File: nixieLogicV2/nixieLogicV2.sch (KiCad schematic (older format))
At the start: 42 parts, among them J1 GPS, J2 Conn_01x10_Female, J3 Barrel_Jack, Q1 2sk3234, SW1 SW_Push, SW2 SW_Push, SW3 SW, SW4 SW, SW5 SW, SW6 SW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

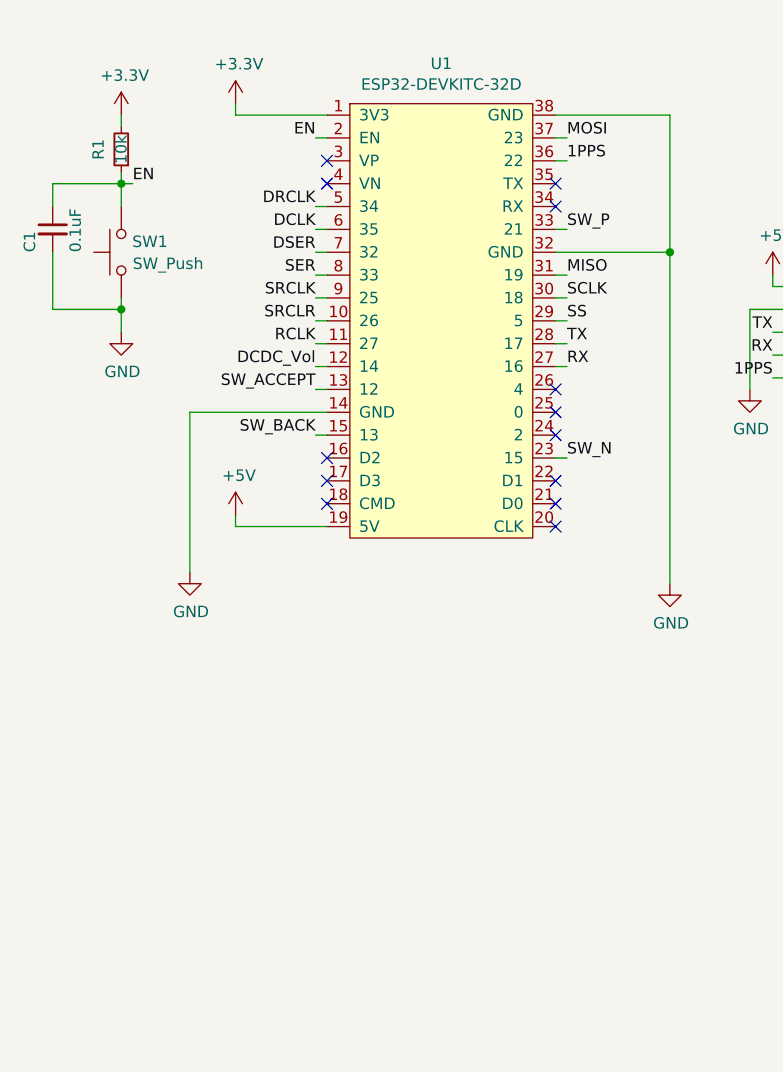
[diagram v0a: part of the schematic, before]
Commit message: add FirmWare Currently Ntp Function working need to add config menu
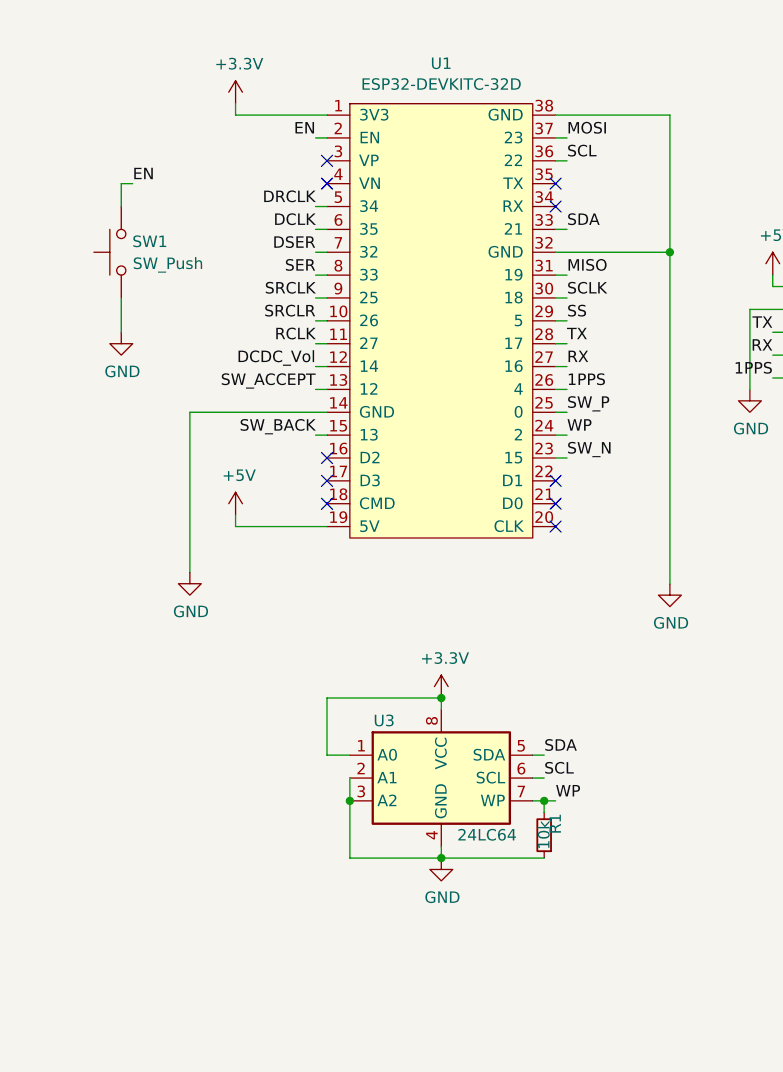
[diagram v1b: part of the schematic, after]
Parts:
- removed C1: 0.1uF, Capacitor_SMD:C_0805_2012Metric_Pad1.15x1.40mm_HandSolder, symbol Device:C_Small
- added U3: 24LC64, Package_DIP:DIP-8_W7.62mm_Socket_LongPads, symbol Memory_EEPROM:24LC64
- D2: footprint Package_TO_SOT_THT:TO-220-2_Horizontal_TabUp -> Package_TO_SOT_THT:TO-220-2_Horizontal_TabDown
- Q1: footprint Package_TO_SOT_THT:TO-220F-3_Horizontal_TabUp -> Package_TO_SOT_THT:TO-220-3_Horizontal_TabDown
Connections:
- net +3V3: now also U3.1 (A0), U3.8 (VCC); no longer R1.2
- net 1PPS: now also U1.26 (4); no longer U1.36 (22)
- net EN: no longer R1.1
- net GND: now also R1.1, U3.2 (A1), U3.3 (A2), U3.4 (GND)
- net SW_P: now also U1.25 (0); no longer U1.33 (21)
- net WP: now reaches U1.24 (2)
- net WP: now also R1.2, U3.7 (WP)
- new net SCL: U1.36 (22), U3.6 (SCL)
- new net SDA: U1.33 (21), U3.5 (SDA)
- no-connect marks 16 -> 13
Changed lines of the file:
@@
 	0    -1   -1   0
 $EndComp
-$Comp
-L Device:C_Small C1
-U 1 1 5FC003DB
-P 4850 1450
-F 0 "C1" V 4750 1350 50  0000 L CNN
-F 1 "0.1uF" V 4950 1350 50  0000 L CNN
-F 2 "Capacitor_SMD:C_0805_2012Metric_Pad1.15x1.40mm_HandSolder" H 4850 1450 50  0001 C CNN
-F 3 "~" H 4850 1450 50  0001 C CNN
-	1    4850 1450
-	1    0    0    -1
-$EndComp
-Wire Wire Line
-	4850 1350 4850 1250
-Wire Wire Line
-	4850 1250 5150 1250
-Wire Wire Line
-	5150 1250 5150 1200
 Wire Wire Line
 	5150 1350 5150 1250
-Connection ~ 5150 1250
-Wire Wire Line
-	4850 1800 5150 1800
-Wire Wire Line
-	5150 1800 5150 1750
 $Comp
 L power:GND #PWR02
@@
 $EndComp
 Wire Wire Line
-	5150 1900 5150 1800
-Connection ~ 5150 1800
-Wire Wire Line
 	5200 1250 5150 1250
-$Comp
-L Device:R_Small R1
-U 1 1 5FC003F2
-P 5150 1100
-F 0 "R1" V 5250 1100 50  0000 C CNN
-F 1 "10k" V 5150 1100 50  0000 C CNN
-F 2 "Resistor_SMD:R_0805_2012Metric_Pad1.15x1.40mm_HandSolder" H 5150 1100 50  0001 C CNN
-F 3 "~" H 5150 1100 50  0001 C CNN
-	1    5150 1100
-	-1   0    0    1
-$EndComp
-Wire Wire Line
-	4850 1550 4850 1800
-$Comp
-L power:+3.3V #PWR01
-U 1 1 5FC003F9
-P 5150 950
-F 0 "#PWR01" H 5150 800 50  0001 C CNN
-F 1 "+3.3V" H 5165 1123 50  0000 C CNN
-F 2 "" H 5150 950 50  0001 C CNN
-F 3 "" H 5150 950 50  0001 C CNN
-	1    5150 950
-	1    0    0    -1
-$EndComp
-Wire Wire Line
-	5150 950  5150 1000
 Text Label 5200 1250 0    50   ~ 0
 EN
@@
 F 0 "Q1" V 9650 1400 50  0000 L CNN
 F 1 "2sk3234" V 9900 1450 50  0000 L CNN
-F 2 "Package_TO_SOT_THT:TO-220F-3_Horizontal_TabUp" H 9900 1700 50  0001 C CNN
+F 2 "Package_TO_SOT_THT:TO-220-3_Horizontal_TabDown" H 9900 1700 50  0001 C CNN
 F 3 "~" H 9700 1600 50  0001 C CNN
 	1    9700 1600
@@
 F 0 "D2" H 10050 583 50  0000 C CNN
 F 1 "SCS206AGC" H 10050 674 50  0000 C CNN
-F 2 "Package_TO_SOT_THT:TO-220-2_Horizontal_TabUp" H 10050 800 50  0001 C CNN
+F 2 "Package_TO_SOT_THT:TO-220-2_Horizontal_TabDown" H 10050 800 50  0001 C CNN
 F 3 "~" H 10050 800 50  0001 C CNN
 	1    10050 800
@@
 Wire Wire Line
 	8000 2100 8050 2100
-Text Label 7100 1150 0    50   ~ 0
+Text Label 7100 2150 0    50   ~ 0
 1PPS
 Wire Wire Line
@@
 Wire Wire Line
 	6050 2150 6000 2150
-Text Label 7100 1450 0    50   ~ 0
+Text Label 7100 2250 0    50   ~ 0
 SW_P
 Wire Wire Line
@@
 Wire Wire Line
 	7100 2450 7050 2450
-NoConn ~ 7050 2350
-NoConn ~ 7050 2250
-NoConn ~ 7050 2150
 Wire Wire Line
 	5650 950  6050 950
@@
 NoConn ~ 9700 3400
 NoConn ~ 8500 2700
+Wire Wire Line
+	5150 1750 5150 1900
+$Comp
+L Memory_EEPROM:24LC64 U3
+U 1 1 5FB93803
+P 6550 3850
+F 0 "U3" H 6300 4100 50  0000 C CNN
+F 1 "24LC64" H 6750 3600 50  0000 C CNN
+F 2 "Package_DIP:DIP-8_W7.62mm_Socket_LongPads" H 6550 3850 50  0001 C CNN
+F 3 "http://ww1.microchip.com/downloads/en/DeviceDoc/21189f.pdf" H 6550 3850 50  0001 C CNN
+	1    6550 3850
+	1    0    0    -1
+$EndComp
+$Comp
+L power:+3.3V #PWR01
+U 1 1 5FB94E4F
+P 6550 3500
+F 0 "#PWR01" H 6550 3350 50  0001 C CNN
+F 1 "+3.3V" H 6565 3673 50  0000 C CNN
+F 2 "" H 6550 3500 50  0001 C CNN
+F 3 "" H 6550 3500 50  0001 C CNN
+	1    6550 3500
+	1    0    0    -1
+$EndComp
+Wire Wire Line
+	6550 3500 6550 3550
+$Comp
+L power:GND #PWR026
+U 1 1 5FBA1D81
+P 6550 4200
+F 0 "#PWR026" H 6550 3950 50  0001 C CNN
+F 1 "GND" H 6555 4027 50  0000 C CNN
+F 2 "" H 6550 4200 50  0001 C CNN
+F 3 "" H 6550 4200 50  0001 C CNN
+	1    6550 4200
+	1    0    0    -1
+$EndComp
+Wire Wire Line
+	6550 4200 6550 4150
+Wire Wire Line
+	6550 3500 6050 3500
+Wire Wire Line
+	6050 3500 6050 3750
+Wire Wire Line
+	6050 3750 6150 3750
+Connection ~ 6550 3500
+Wire Wire Line
+	6150 3850 6150 3950
+Wire Wire Line
+	6150 3950 6150 4200
+Wire Wire Line
+	6150 4200 6550 4200
+Connection ~ 6150 3950
+Connection ~ 6550 4200
+$Comp
+L Device:R_Small R1
+U 1 1 5FBF9365
+P 7000 4100
+F 0 "R1" V 6950 4050 50  0000 C CNN
+F 1 "10k" V 7000 4100 50  0000 C CNN
+F 2 "Resistor_SMD:R_0805_2012Metric_Pad1.15x1.40mm_HandSolder" H 7000 4100 50  0001 C CNN
+F 3 "~" H 7000 4100 50  0001 C CNN
+	1    7000 4100
+	-1   0    0    1
+$EndComp
+Wire Wire Line
+	7000 4000 7000 3950
+Wire Wire Line
+	7000 3950 6950 3950
+Wire Wire Line
+	7000 4200 6550 4200
+Wire Wire Line
+	7100 2250 7050 2250
+Wire Wire Line
+	7100 2150 7050 2150
+Text Label 7050 3950 0    50   ~ 0
+WP
+Wire Wire Line
+	7050 3950 7000 3950
+Connection ~ 7000 3950
+Text Label 7100 2350 0    50   ~ 0
+WP
+Wire Wire Line
+	7100 2350 7050 2350
+Text Label 7000 3850 0    50   ~ 0
+SCL
+Wire Wire Line
+	7000 3850 6950 3850
+Text Label 7100 1150 0    50   ~ 0
+SCL
+Wire Wire Line
+	7000 3750 6950 3750
+Text Label 7000 3750 0    50   ~ 0
+SDA
+Text Label 7100 1450 0    50   ~ 0
+SDA
 $EndSCHEMATC
